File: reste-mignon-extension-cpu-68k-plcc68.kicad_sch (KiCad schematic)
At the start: 20 parts, among them J1 RESTE_MIGNON_CPU_CONNECTOR_A, J2 RESTE_MIGNON_CPU_CONNECTOR_B, U1 MC68000_PLCC_68_PHY

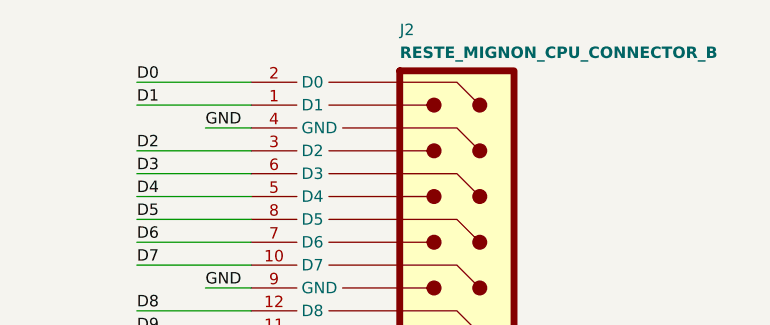
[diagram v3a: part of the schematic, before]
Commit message: pcb session -- laying out component -- fixed footprint associations
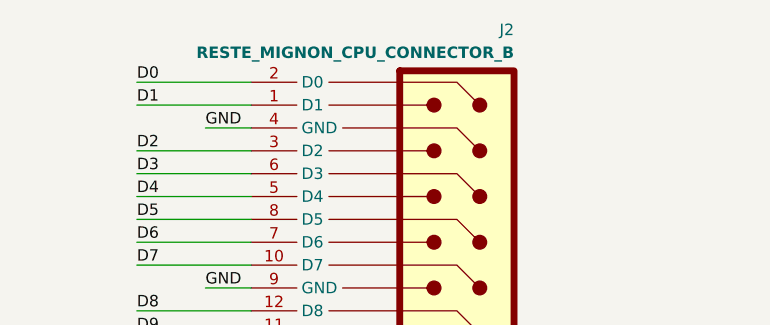
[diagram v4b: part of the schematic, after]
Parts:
- J2: footprint Connector_PinHeader_2.54mm:PinHeader_2x14_P2.54mm_Vertical -> Connector_PinHeader_2.54mm:PinHeader_2x16_P2.54mm_Vertical
- JP1: footprint Connector_PinHeader_2.54mm:PinHeader_2x24_P2.54mm_Vertical -> Jumper:SolderJumper-2_P1.3mm_Bridged_RoundedPad1.0x1.5mm
- JP2: footprint Connector_PinHeader_2.54mm:PinHeader_2x16_P2.54mm_Vertical -> Jumper:SolderJumper-2_P1.3mm_Bridged_RoundedPad1.0x1.5mm
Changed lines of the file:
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@@
       (effects (font (size 1.27 1.27)) (justify left))
     )
-    (property "Footprint" "Connector_PinHeader_2.54mm:PinHeader_2x24_P2.54mm_Vertical" (at 40.64 177.8 0)
+    (property "Footprint" "Jumper:SolderJumper-2_P1.3mm_Bridged_RoundedPad1.0x1.5mm" (at 40.64 177.8 0)
       (effects (font (size 1.27 1.27)) hide)
     )
@@
       (effects (font (size 1.27 1.27)) (justify left))
     )
-    (property "Footprint" "Connector_PinHeader_2.54mm:PinHeader_2x16_P2.54mm_Vertical" (at 40.64 180.34 0)
+    (property "Footprint" "Jumper:SolderJumper-2_P1.3mm_Bridged_RoundedPad1.0x1.5mm" (at 40.64 180.34 0)
       (effects (font (size 1.27 1.27)) hide)
     )
@@
   (symbol (lib_id "reste-mignon-interconnect:CPU_Connector_B") (at 185.42 25.4 0) (unit 1)
     (in_bom yes) (on_board yes) (dnp no)
-    (property "Reference" "J2" (at 181.61 17.78 0)
-      (effects (font (size 1.27 1.27)) (justify left bottom))
-    )
-    (property "Value" "RESTE_MIGNON_CPU_CONNECTOR_B" (at 181.61 20.32 0)
-      (effects (font (size 1.27 1.27) bold) (justify left bottom))
-    )
-    (property "Footprint" "Connector_PinHeader_2.54mm:PinHeader_2x14_P2.54mm_Vertical" (at 185.42 14.986 0)
-      (effects (font (size 1.27 1.27)) hide)
-    )
+    (property "Reference" "J2" (at 194.31 17.78 0)
+      (effects (font (size 1.27 1.27)) (justify right bottom))
+    )
+    (property "Value" "RESTE_MIGNON_CPU_CONNECTOR_B" (at 194.31 20.32 0)
+      (effects (font (size 1.27 1.27) bold) (justify right bottom))
+    )
+    (property "Footprint" "Connector_PinHeader_2.54mm:PinHeader_2x16_P2.54mm_Vertical" (at 185.42 14.986 0)
+      (effects (font (size 1.27 1.27)) hide)
+    )

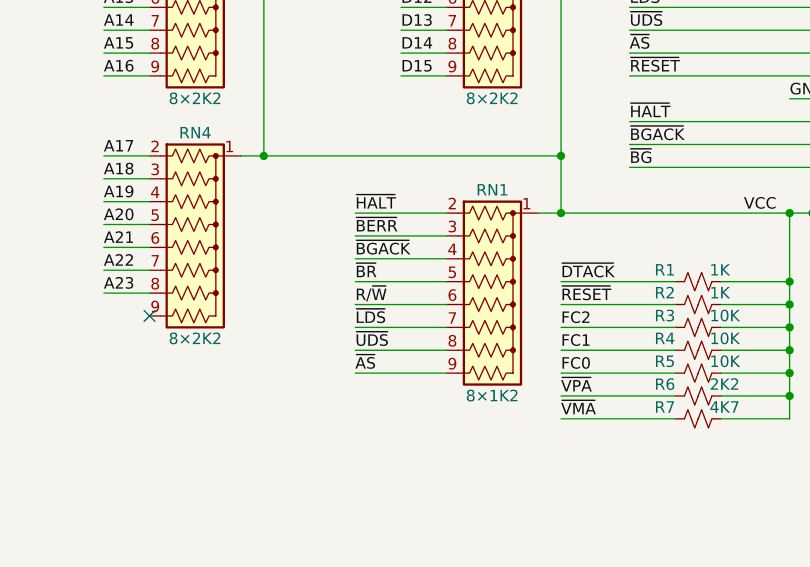
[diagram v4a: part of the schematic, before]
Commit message: pcb session -- start pull-ups, adjust pull-up mapping of RN1 for ease of routing
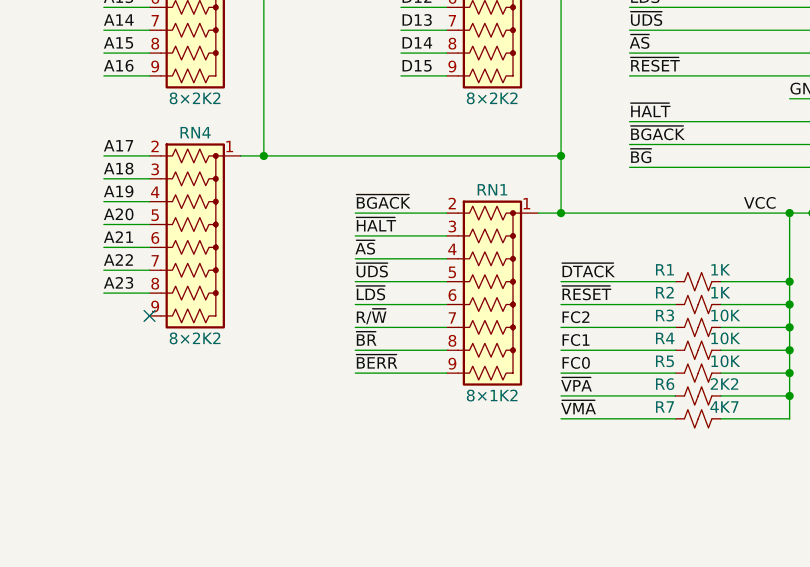
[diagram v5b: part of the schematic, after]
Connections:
- net R/~{W}: now also RN1.7 (R6); no longer RN1.6 (R5)
- net ~{AS}: now also RN1.4 (R3); no longer RN1.9 (R8)
- net ~{BERR}: now also RN1.9 (R8); no longer RN1.3 (R2)
- net ~{BGACK}: now also RN1.2 (R1); no longer RN1.4 (R3)
- net ~{BR}: now also RN1.8 (R7); no longer RN1.5 (R4)
- net ~{HALT}: now also RN1.3 (R2); no longer RN1.2 (R1)
- net ~{LDS}: now also RN1.6 (R5); no longer RN1.7 (R6)
- net ~{UDS}: now also RN1.5 (R4); no longer RN1.8 (R7)
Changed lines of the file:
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@@
     (effects (font (size 1.27 1.27)) (justify left bottom))
   )
-  (label "~{LDS}" (at 111.76 114.3 0) (fields_autoplaced)
+  (label "~{LDS}" (at 111.76 111.76 0) (fields_autoplaced)
     (effects (font (size 1.27 1.27)) (justify left bottom))
   )
@@
     (effects (font (size 1.27 1.27)) (justify right bottom))
   )
-  (label "~{BERR}" (at 111.76 104.14 0) (fields_autoplaced)
+  (label "~{BERR}" (at 111.76 119.38 0) (fields_autoplaced)
     (effects (font (size 1.27 1.27)) (justify left bottom))
   )
@@
     (effects (font (size 1.27 1.27)) (justify left bottom))
   )
-  (label "~{BR}" (at 111.76 109.22 0) (fields_autoplaced)
+  (label "~{BR}" (at 111.76 116.84 0) (fields_autoplaced)
     (effects (font (size 1.27 1.27)) (justify left bottom))
   )
@@
     (effects (font (size 1.27 1.27)) (justify right bottom))
   )
-  (label "~{BGACK}" (at 111.76 106.68 0) (fields_autoplaced)
+  (label "~{BGACK}" (at 111.76 101.6 0) (fields_autoplaced)
     (effects (font (size 1.27 1.27)) (justify left bottom))
   )
@@
     (effects (font (size 1.27 1.27)) (justify left bottom))
   )
-  (label "R{slash}~{W}" (at 111.76 111.76 0) (fields_autoplaced)
+  (label "R{slash}~{W}" (at 111.76 114.3 0) (fields_autoplaced)
     (effects (font (size 1.27 1.27)) (justify left bottom))
   )
@@
     (effects (font (size 1.27 1.27)) (justify left bottom))
   )
-  (label "~{UDS}" (at 111.76 116.84 0) (fields_autoplaced)
+  (label "~{UDS}" (at 111.76 109.22 0) (fields_autoplaced)
     (effects (font (size 1.27 1.27)) (justify left bottom))
   )
@@
     (effects (font (size 1.27 1.27)) (justify right bottom))
   )
-  (label "~{HALT}" (at 111.76 101.6 0) (fields_autoplaced)
+  (label "~{HALT}" (at 111.76 104.14 0) (fields_autoplaced)
     (effects (font (size 1.27 1.27)) (justify left bottom))
   )
@@
     (effects (font (size 1.27 1.27)) (justify left bottom))
   )
-  (label "~{AS}" (at 111.76 119.38 0) (fields_autoplaced)
-    (effects (font (size 1.27 1.27)) (justify left bottom))
-  )
+  (label "~{AS}" (at 111.76 106.68 0) (fields_autoplaced)
+    (effects (font (size 1.27 1.27)) (justify left bottom))
+  )

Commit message: pcb session -- continue pull-ups, done a1-a12
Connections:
- net A17: now also RN4.8 (R7); no longer RN4.2 (R1)
- net A18: now also RN4.7 (R6); no longer RN4.3 (R2)
- net A19: now also RN4.6 (R5); no longer RN4.4 (R3)
- net A21: now also RN4.4 (R3); no longer RN4.6 (R5)
- net A22: now also RN4.3 (R2); no longer RN4.7 (R6)
- net A23: now also RN4.2 (R1); no longer RN4.8 (R7)
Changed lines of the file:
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@@
     (effects (font (size 1.27 1.27)) (justify left bottom))
   )
-  (label "A21" (at 83.82 105.41 0) (fields_autoplaced)
+  (label "A21" (at 83.82 100.33 0) (fields_autoplaced)
     (effects (font (size 1.27 1.27)) (justify left bottom))
   )
@@
     (effects (font (size 1.27 1.27)) (justify left bottom))
   )
-  (label "A23" (at 83.82 110.49 0) (fields_autoplaced)
+  (label "A23" (at 83.82 95.25 0) (fields_autoplaced)
     (effects (font (size 1.27 1.27)) (justify left bottom))
   )
@@
     (effects (font (size 1.27 1.27)) (justify left bottom))
   )
-  (label "A17" (at 83.82 95.25 0) (fields_autoplaced)
+  (label "A17" (at 83.82 110.49 0) (fields_autoplaced)
     (effects (font (size 1.27 1.27)) (justify left bottom))
   )
@@
     (effects (font (size 1.27 1.27)) (justify left bottom))
   )
-  (label "A18" (at 83.82 97.79 0) (fields_autoplaced)
+  (label "A18" (at 83.82 107.95 0) (fields_autoplaced)
     (effects (font (size 1.27 1.27)) (justify left bottom))
   )
@@
     (effects (font (size 1.27 1.27)) (justify left bottom))
   )
-  (label "A22" (at 83.82 107.95 0) (fields_autoplaced)
+  (label "A22" (at 83.82 97.79 0) (fields_autoplaced)
     (effects (font (size 1.27 1.27)) (justify left bottom))
   )
@@
     (effects (font (size 1.27 1.27)) (justify left bottom))
   )
-  (label "A19" (at 83.82 100.33 0) (fields_autoplaced)
-    (effects (font (size 1.27 1.27)) (justify left bottom))
-  )
+  (label "A19" (at 83.82 105.41 0) (fields_autoplaced)
+    (effects (font (size 1.27 1.27)) (justify left bottom))
+  )

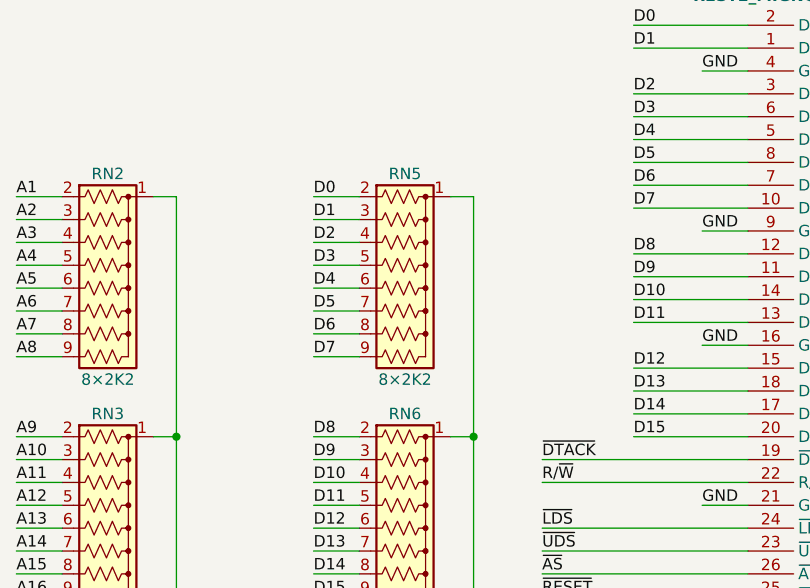
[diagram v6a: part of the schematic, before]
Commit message: switch RN5 and RN6 to ease routing
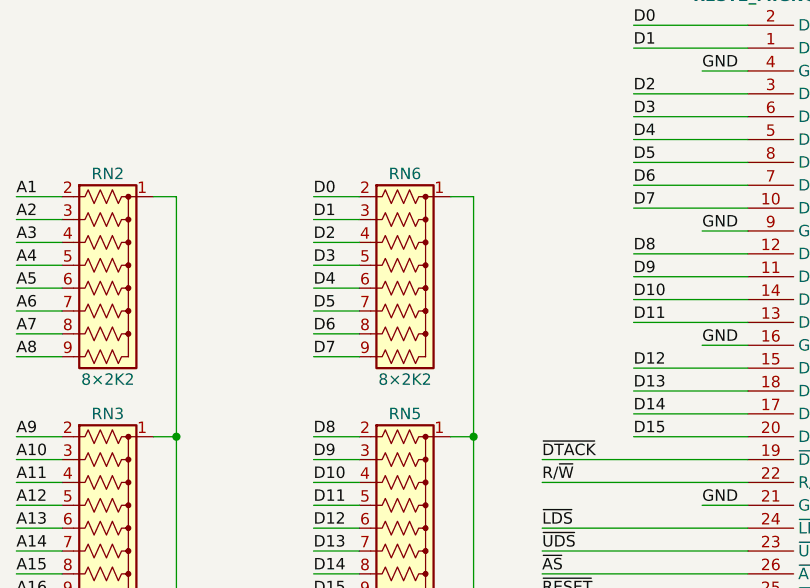
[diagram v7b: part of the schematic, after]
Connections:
- net D0: now also RN6.2 (R1); no longer RN5.2 (R1)
- net D1: now also RN6.3 (R2); no longer RN5.3 (R2)
- net D10: now also RN5.4 (R3); no longer RN6.4 (R3)
- net D11: now also RN5.5 (R4); no longer RN6.5 (R4)
- net D12: now also RN5.6 (R5); no longer RN6.6 (R5)
- net D13: now also RN5.7 (R6); no longer RN6.7 (R6)
- net D14: now also RN5.8 (R7); no longer RN6.8 (R7)
- net D15: now also RN5.9 (R8); no longer RN6.9 (R8)
- net D2: now also RN6.4 (R3); no longer RN5.4 (R3)
- net D3: now also RN6.5 (R4); no longer RN5.5 (R4)
- net D4: now also RN6.6 (R5); no longer RN5.6 (R5)
- net D5: now also RN6.7 (R6); no longer RN5.7 (R6)
- net D6: now also RN6.8 (R7); no longer RN5.8 (R7)
- net D7: now also RN6.9 (R8); no longer RN5.9 (R8)
- net D8: now also RN5.2 (R1); no longer RN6.2 (R1)
- net D9: now also RN5.3 (R2); no longer RN6.3 (R2)
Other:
- moved on the sheet: RN5, RN6
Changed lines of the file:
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@@
     )
   )
-  (symbol (lib_id "Device:R_Network08_US") (at 127 52.07 270) (unit 1)
-    (in_bom yes) (on_board yes) (dnp no)
-    (property "Reference" "RN5" (at 127 39.37 90)
-      (effects (font (size 1.27 1.27)))
-    )
-    (property "Value" "8×2K2" (at 127 62.23 90)
-      (effects (font (size 1.27 1.27)))
-    )
-    (property "Footprint" "Resistor_THT:R_Array_SIP9" (at 127 64.135 90)
-      (effects (font (size 1.27 1.27)) hide)
-    )
-    (property "Datasheet" "http://www.vishay.com/docs/31509/csc.pdf" (at 127 52.07 0)
+  (symbol (lib_id "Device:R_Network08_US") (at 127 78.74 270) (unit 1)
+    (in_bom yes) (on_board yes) (dnp no)
+    (property "Reference" "RN5" (at 127 66.04 90)
+      (effects (font (size 1.27 1.27)))
+    )
+    (property "Value" "8×2K2" (at 127 88.9 90)
+      (effects (font (size 1.27 1.27)))
+    )
+    (property "Footprint" "Resistor_THT:R_Array_SIP9" (at 127 90.805 90)
+      (effects (font (size 1.27 1.27)) hide)
+    )
+    (property "Datasheet" "http://www.vishay.com/docs/31509/csc.pdf" (at 127 78.74 0)
       (effects (font (size 1.27 1.27)) hide)
     )
@@
     )
   )
-  (symbol (lib_id "Device:R_Network08_US") (at 127 78.74 270) (unit 1)
-    (in_bom yes) (on_board yes) (dnp no)
-    (property "Reference" "RN6" (at 127 66.04 90)
-      (effects (font (size 1.27 1.27)))
-    )
-    (property "Value" "8×2K2" (at 127 88.9 90)
-      (effects (font (size 1.27 1.27)))
-    )
-    (property "Footprint" "Resistor_THT:R_Array_SIP9" (at 127 90.805 90)
-      (effects (font (size 1.27 1.27)) hide)
-    )
-    (property "Datasheet" "http://www.vishay.com/docs/31509/csc.pdf" (at 127 78.74 0)
-      (effects (font (size 1.27 1.27)) hide)
-    )
+  (symbol (lib_id "Device:R_Network08_US") (at 127 52.07 270) (unit 1)
+    (in_bom yes) (on_board yes) (dnp no)
+    (property "Reference" "RN6" (at 127 39.37 90)
+      (effects (font (size 1.27 1.27)))
+    )
+    (property "Value" "8×2K2" (at 127 62.23 90)
+      (effects (font (size 1.27 1.27)))
+    )
+    (property "Footprint" "Resistor_THT:R_Array_SIP9" (at 127 64.135 90)
+      (effects (font (size 1.27 1.27)) hide)
+    )
+    (property "Datasheet" "http://www.vishay.com/docs/31509/csc.pdf" (at 127 52.07 0)
+      (effects (font (size 1.27 1.27)) hide)
+    )
